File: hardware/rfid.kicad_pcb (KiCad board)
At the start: 2 copper layers, 29 parts, among them P1 CONN_01X02, P2 COMMS, U1 CR95HF, X1 27.12MHz

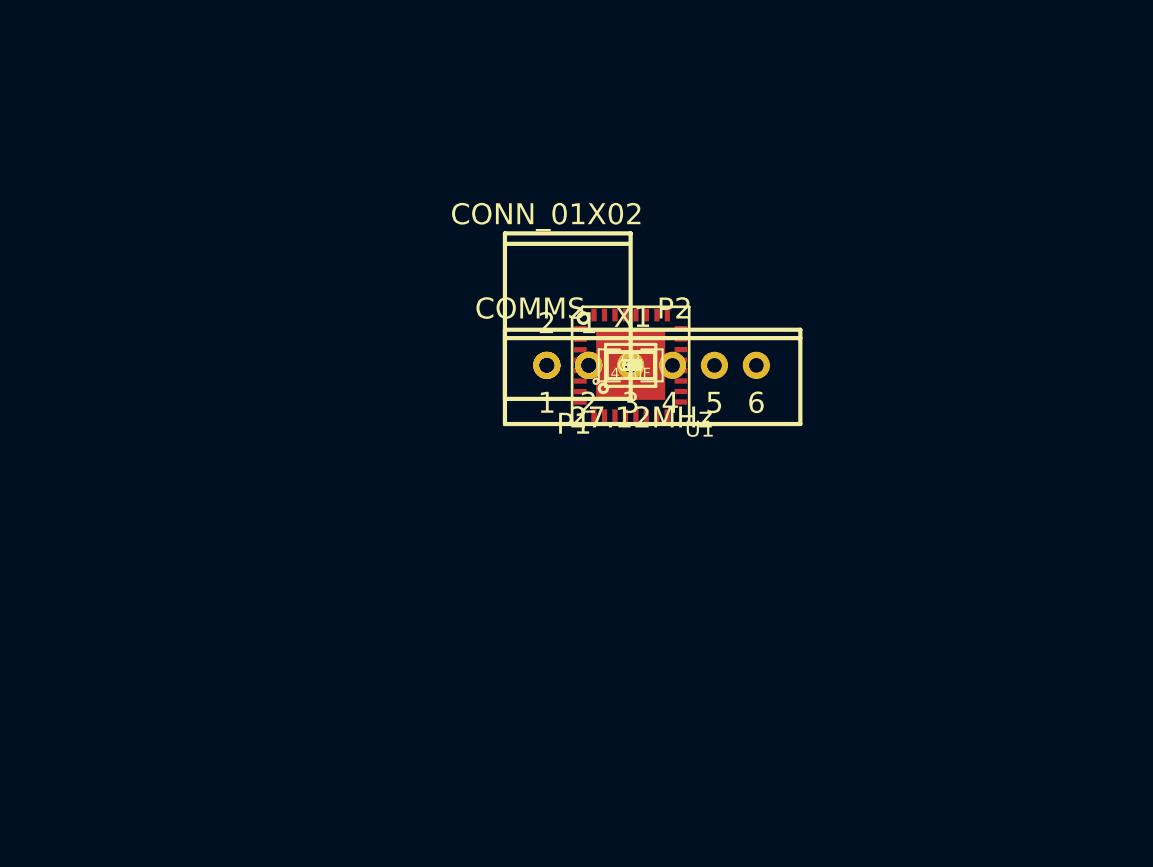
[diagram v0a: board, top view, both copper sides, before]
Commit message: Started placing components on PCB. They are just spread out currently.
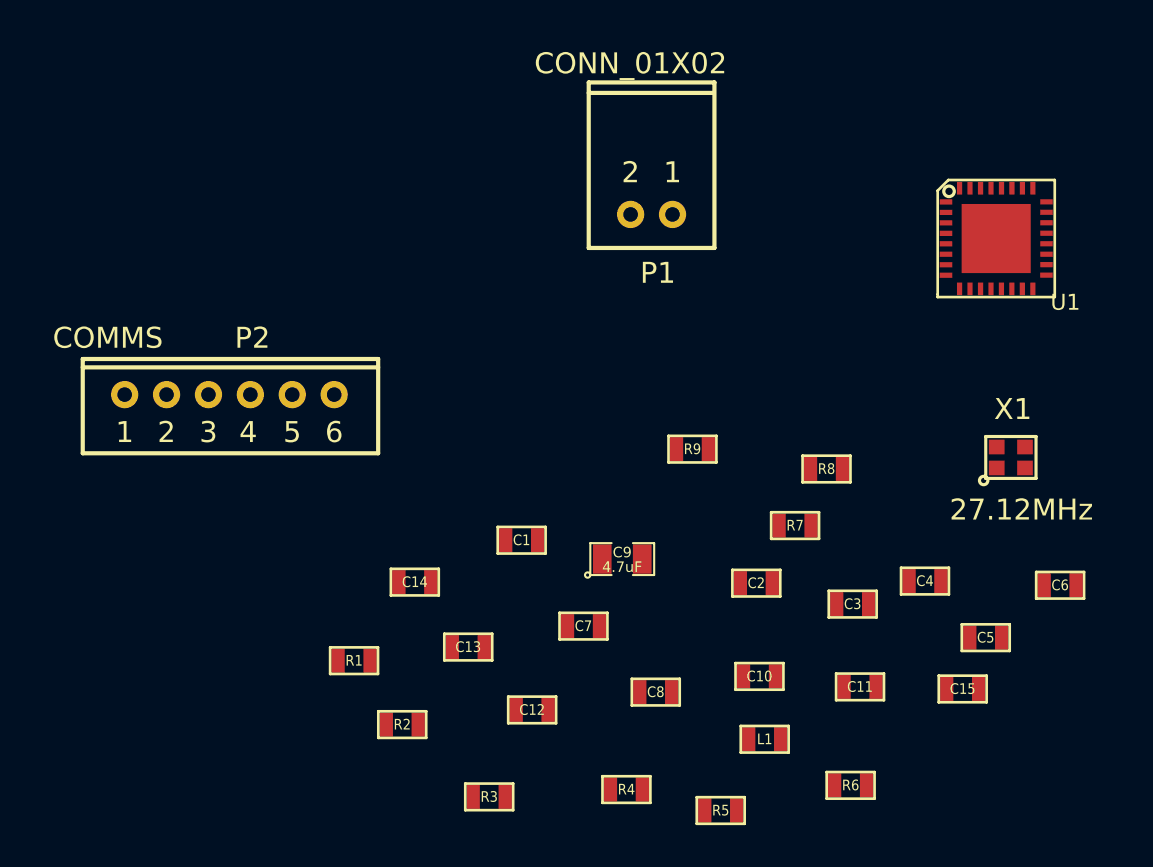
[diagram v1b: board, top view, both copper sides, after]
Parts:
- moved C6 23.0 mm to (169.0, 115.5)
- moved R6 22.6 mm to (159.0, 125.0)
- moved C15 22.1 mm to (164.3, 120.5)
- moved R5 21.7 mm to (152.8, 126.2)
- moved R3 21.7 mm to (141.8, 125.6)
- moved C5 21.4 mm to (165.4, 118.0)
- moved R2 20.3 mm to (137.6, 122.2)
- moved R4 20.2 mm to (148.3, 125.2)
- moved P2 20.2 mm to (128.3, 106.4)
- moved R1 19.3 mm to (135.3, 119.1)
- moved L1 19.0 mm to (154.9, 122.8)
- moved C11 18.9 mm to (159.4, 120.3)
- moved X1 18.7 mm to (166.7, 109.4)
- moved U1 18.5 mm to (165.9, 99.0)
- moved C4 17.4 mm to (162.6, 115.3)
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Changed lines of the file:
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@@
 (kicad_pcb (version 4) (host pcbnew "(2014-09-17 BZR 5140)-product")
   (general
-    (links 0)
-    (no_connects 0)
-    (area 0 0 0 0)
+    (links 60)
+    (no_connects 33)
+    (area 139.338767 96.6246 156.955101 108.9025)
     (thickness 1.6)
     (drawings 0)
@@
     (uvia_dia 0.508)
     (uvia_drill 0.127)
-  )
-  (module SMD_Packages:SMD-0603 (layer F.Cu)
-    (at 148.5011 105.0036)
+    (add_net 3V3)
+    (add_net 3V3_RF)
+    (add_net GND)
+    (add_net "Net-(C1-Pad1)")
+    (add_net "Net-(C10-Pad2)")
+    (add_net "Net-(C11-Pad2)")
+    (add_net "Net-(C12-Pad1)")
+    (add_net "Net-(C13-Pad1)")
+    (add_net "Net-(C2-Pad1)")
+    (add_net "Net-(C7-Pad1)")
+    (add_net "Net-(P2-Pad1)")
+    (add_net "Net-(P2-Pad2)")
+    (add_net "Net-(P2-Pad3)")
+    (add_net "Net-(P2-Pad4)")
+    (add_net "Net-(P2-Pad5)")
+    (add_net "Net-(P2-Pad6)")
+    (add_net "Net-(R2-Pad1)")
+    (add_net "Net-(R3-Pad1)")
+    (add_net "Net-(R5-Pad2)")
+    (add_net "Net-(R6-Pad2)")
+    (add_net "Net-(R7-Pad2)")
+    (add_net "Net-(R8-Pad2)")
+    (add_net "Net-(U1-Pad10)")
+    (add_net "Net-(U1-Pad11)")
+    (add_net "Net-(U1-Pad23)")
+    (add_net "Net-(U1-Pad24)")
+    (add_net "Net-(U1-Pad25)")
+    (add_net "Net-(U1-Pad26)")
+    (add_net "Net-(U1-Pad27)")
+    (add_net "Net-(U1-Pad28)")
+    (add_net "Net-(U1-Pad3)")
+    (add_net "Net-(U1-Pad4)")
+    (add_net "Net-(U1-Pad7)")
+    (add_net "Net-(X1-Pad2)")
+    (add_net "Net-(X1-Pad4)")
+  )
+  (module SMD_Packages:SMD-0603 (layer F.Cu)
+    (at 143.3 113.35)
     (attr smd)
     (fp_text reference C1 (at 0 0) (layer F.SilkS)
@@
   )
   (module SMD_Packages:SMD-0603 (layer F.Cu)
-    (at 148.5011 105.0036)
+    (at 154.5 115.4)
     (attr smd)
     (fp_text reference C2 (at 0 0) (layer F.SilkS)
@@
   )
   (module SMD_Packages:SMD-0603 (layer F.Cu)
-    (at 148.5011 105.0036)
+    (at 159.1 116.4)
     (attr smd)
     (fp_text reference C3 (at 0 0) (layer F.SilkS)
@@
   )
   (module SMD_Packages:SMD-0603 (layer F.Cu)
-    (at 148.5011 105.0036)
+    (at 162.55 115.3)
     (attr smd)
     (fp_text reference C4 (at 0 0) (layer F.SilkS)
@@
   )
   (module SMD_Packages:SMD-0603 (layer F.Cu)
-    (at 148.5011 105.0036)
+    (at 165.45 118)
     (attr smd)
     (fp_text reference C5 (at 0 0) (layer F.SilkS)
@@
   )
   (module SMD_Packages:SMD-0603 (layer F.Cu)
-    (at 148.5011 105.0036)
+    (at 169 115.5)
     (attr smd)
     (fp_text reference C6 (at 0 0) (layer F.SilkS)
@@
   )
   (module SMD_Packages:SMD-0603 (layer F.Cu)
-    (at 148.5011 105.0036)
+    (at 146.25 117.45)
     (attr smd)
     (fp_text reference C7 (at 0 0) (layer F.SilkS)
@@
   )
   (module SMD_Packages:SMD-0603 (layer F.Cu)
-    (at 148.5011 105.0036)
+    (at 149.7 120.6)
     (attr smd)
     (fp_text reference C8 (at 0 0) (layer F.SilkS)
@@
   )
   (module SMD_Packages:SMD-0805 (layer F.Cu)
-    (at 148.5011 105.0036)
+    (at 148.1 114.25)
     (attr smd)
     (fp_text reference C9 (at 0 -0.3175) (layer F.SilkS)
@@
   )
   (module SMD_Packages:SMD-0603 (layer F.Cu)
-    (at 148.5011 105.0036)
+    (at 154.65 119.85)
     (attr smd)
     (fp_text reference C10 (at 0 0) (layer F.SilkS)
@@
   )
   (module SMD_Packages:SMD-0603 (layer F.Cu)
-    (at 148.5011 105.0036)
+    (at 159.45 120.35)
     (attr smd)
     (fp_text reference C11 (at 0 0) (layer F.SilkS)
@@
   )
   (module SMD_Packages:SMD-0603 (layer F.Cu)
-    (at 148.5011 105.0036)
+    (at 143.8 121.45)
     (attr smd)
     (fp_text reference C12 (at 0 0) (layer F.SilkS)
@@
   )
   (module SMD_Packages:SMD-0603 (layer F.Cu)
-    (at 148.5011 105.0036)
+    (at 140.75 118.45)
     (attr smd)
     (fp_text reference C13 (at 0 0) (layer F.SilkS)
@@
   )
   (module SMD_Packages:SMD-0603 (layer F.Cu)
-    (at 148.5011 105.0036)
+    (at 138.2 115.35)
     (attr smd)
     (fp_text reference C14 (at 0 0) (layer F.SilkS)
@@
   )
   (module SMD_Packages:SMD-0603 (layer F.Cu)
-    (at 148.5011 105.0036)
+    (at 164.35 120.45)
     (attr smd)
     (fp_text reference C15 (at 0 0) (layer F.SilkS)
@@
   )
   (module SMD_Packages:SMD-0603 (layer F.Cu)
-    (at 148.5011 105.0036)
+    (at 154.9 122.85)
     (attr smd)
     (fp_text reference L1 (at 0 0) (layer F.SilkS)
@@
   )
   (module rfid:JST_PH_2pin_side (layer F.Cu)
-    (at 148.5011 105.0036)
+    (at 152.5 97.8)
     (fp_text reference P1 (at -2.7 2.8) (layer F.SilkS)
       (effects (font (size 1 1) (thickness 0.15)))
@@
   )
   (module rfid:JST_PH_6pin (layer F.Cu)
-    (at 148.5011 105.0036)
+    (at 128.35 106.4)
     (fp_text reference P2 (at 2.1 -2.7) (layer F.SilkS)
       (effects (font (size 1 1) (thickness 0.15)))
@@
   )
   (module SMD_Packages:SMD-0603 (layer F.Cu)
-    (at 148.5011 105.0036)
+    (at 135.3 119.1)
     (attr smd)
     (fp_text reference R1 (at 0 0) (layer F.SilkS)
@@
   )
   (module SMD_Packages:SMD-0603 (layer F.Cu)
-    (at 148.5011 105.0036)
+    (at 137.6 122.15)
     (attr smd)
     (fp_text reference R2 (at 0 0) (layer F.SilkS)
@@
   )
   (module SMD_Packages:SMD-0603 (layer F.Cu)
-    (at 148.5011 105.0036)
+    (at 141.75 125.6)
     (attr smd)
     (fp_text reference R3 (at 0 0) (layer F.SilkS)
@@
   )
   (module SMD_Packages:SMD-0603 (layer F.Cu)
-    (at 148.5011 105.0036)
+    (at 148.3 125.25)
     (attr smd)
     (fp_text reference R4 (at 0 0) (layer F.SilkS)
@@
   )
   (module SMD_Packages:SMD-0603 (layer F.Cu)
-    (at 148.5011 105.0036)
+    (at 152.8 126.25)
     (attr smd)
     (fp_text reference R5 (at 0 0) (layer F.SilkS)
@@
   )
   (module SMD_Packages:SMD-0603 (layer F.Cu)
-    (at 148.5011 105.0036)
+    (at 159 125.05)
     (attr smd)
     (fp_text reference R6 (at 0 0) (layer F.SilkS)
@@
   )
   (module SMD_Packages:SMD-0603 (layer F.Cu)
-    (at 148.5011 105.0036)
+    (at 156.35 112.65)
     (attr smd)
     (fp_text reference R7 (at 0 0) (layer F.SilkS)
@@
   )
   (module SMD_Packages:SMD-0603 (layer F.Cu)
-    (at 148.5011 105.0036)
+    (at 157.85 109.95)
     (attr smd)
     (fp_text reference R8 (at 0 0) (layer F.SilkS)
@@
   )
   (module SMD_Packages:SMD-0603 (layer F.Cu)
-    (at 148.5011 105.0036)
+    (at 151.4511 109.0036)
     (attr smd)
     (fp_text reference R9 (at 0 0) (layer F.SilkS)
@@
   )
   (module SMD_Packages:QFN-32-1EP (layer F.Cu)
-    (at 148.5011 105.0036)
+    (at 165.95 98.95)
     (descr QFN-32-1EP)
     (attr smd)
@@
   )
   (module rfid:2x1.6_crystal (layer F.Cu)
-    (at 148.5011 105.0036)
+    (at 166.65 109.4)
     (fp_text reference X1 (at 0.1 -2.3) (layer F.SilkS)
       (effects (font (size 1 1) (thickness 0.15)))

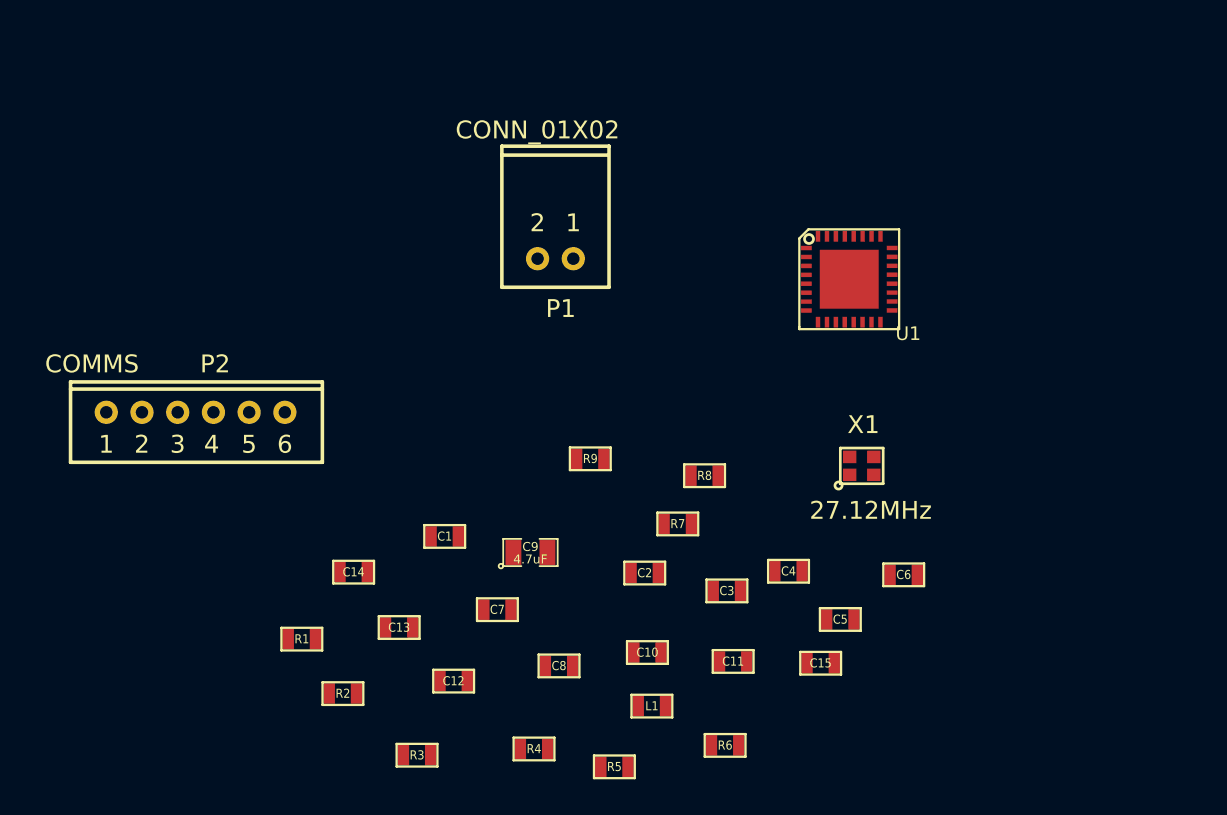
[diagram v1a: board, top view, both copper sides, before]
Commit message: Moved components around on rfid board. They are kinda where they need to go now. Need to figure out what size PCB should be before anything else.
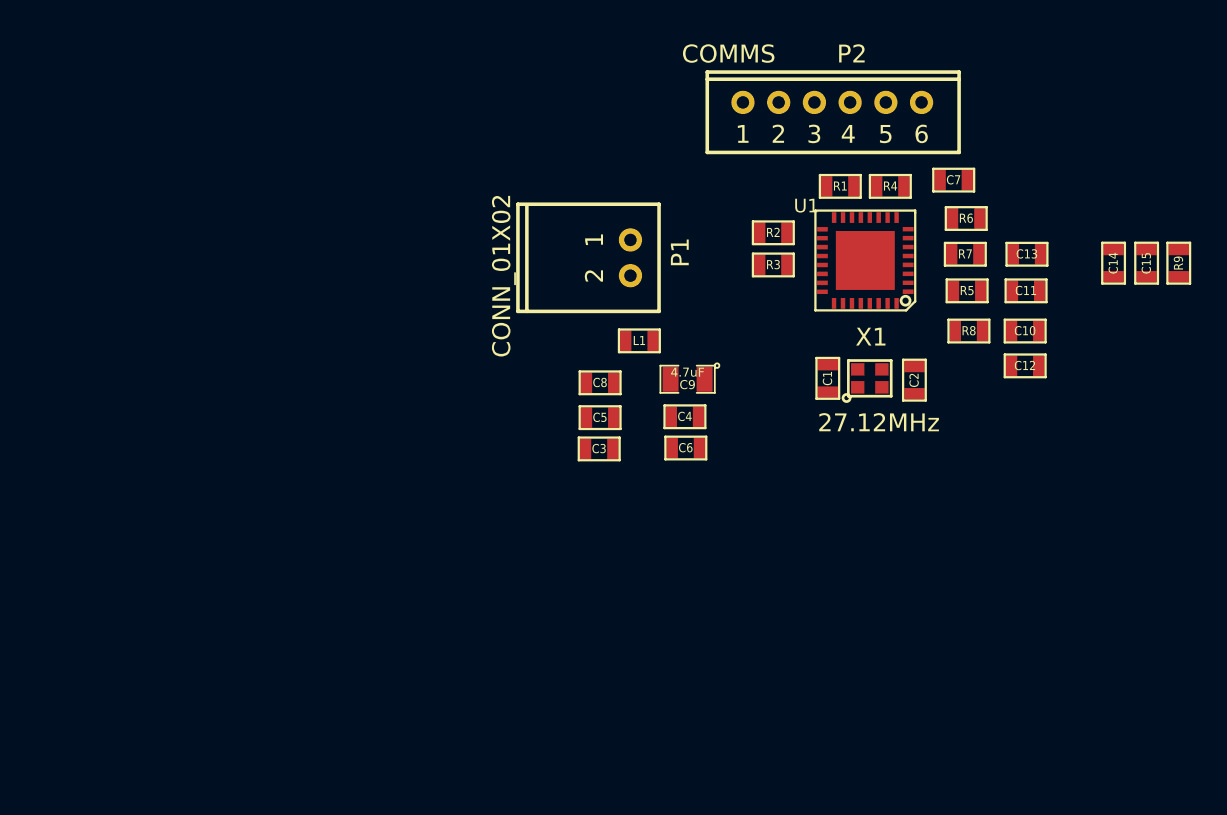
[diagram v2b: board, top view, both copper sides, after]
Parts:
- moved C14 45.9 mm to (180.8, 98.0), turned to 90 degrees
- moved C13 40.9 mm to (175.9, 97.5), turned to 180 degrees
- moved P2 39.6 mm to (164.0, 89.0)
- moved R1 39.4 mm to (165.4, 93.8), turned to 180 degrees
- moved R4 37.3 mm to (168.2, 93.8)
- moved C12 36.5 mm to (175.8, 103.8), turned to 180 degrees
- moved R2 35.3 mm to (161.7, 96.3), turned to 180 degrees
- moved C7 35.1 mm to (171.8, 93.4)
- moved R9 34.7 mm to (184.4, 98.0), turned to 90 degrees
- moved R3 33.9 mm to (161.7, 98.2), turned to 180 degrees
- moved R5 33.2 mm to (172.6, 99.6), turned to 180 degrees
- moved R6 32.4 mm to (172.5, 95.5), turned to 180 degrees
- moved C15 28.9 mm to (182.6, 98.0), turned to 90 degrees
- moved C10 27.8 mm to (175.8, 101.8), turned to 180 degrees
- moved C11 26.4 mm to (175.8, 99.6), turned to 180 degrees
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
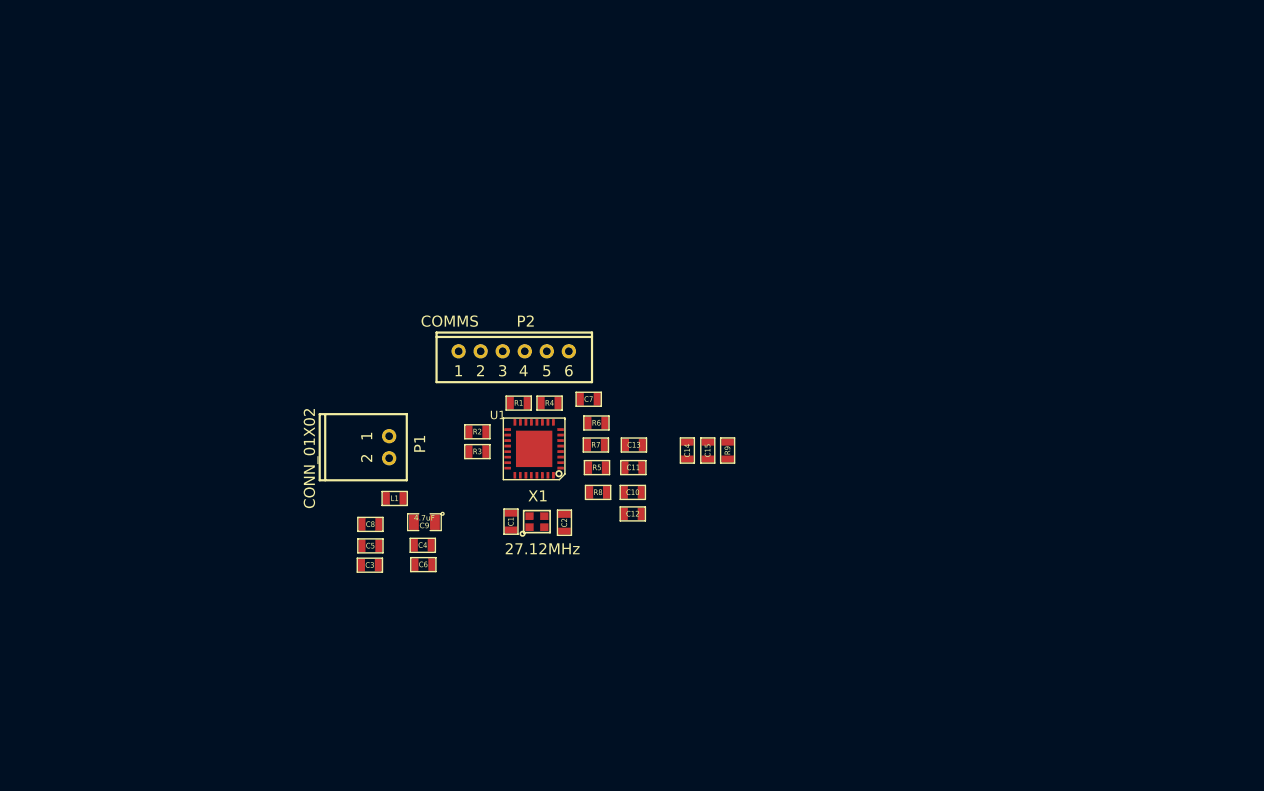
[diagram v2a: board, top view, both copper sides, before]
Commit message: Created board outline for rfid board (5cmX7.5cm). Added four 3.5mm mounting holes on a 4cmX6.5cm centers. Added ~420nH square antenna to board as well.
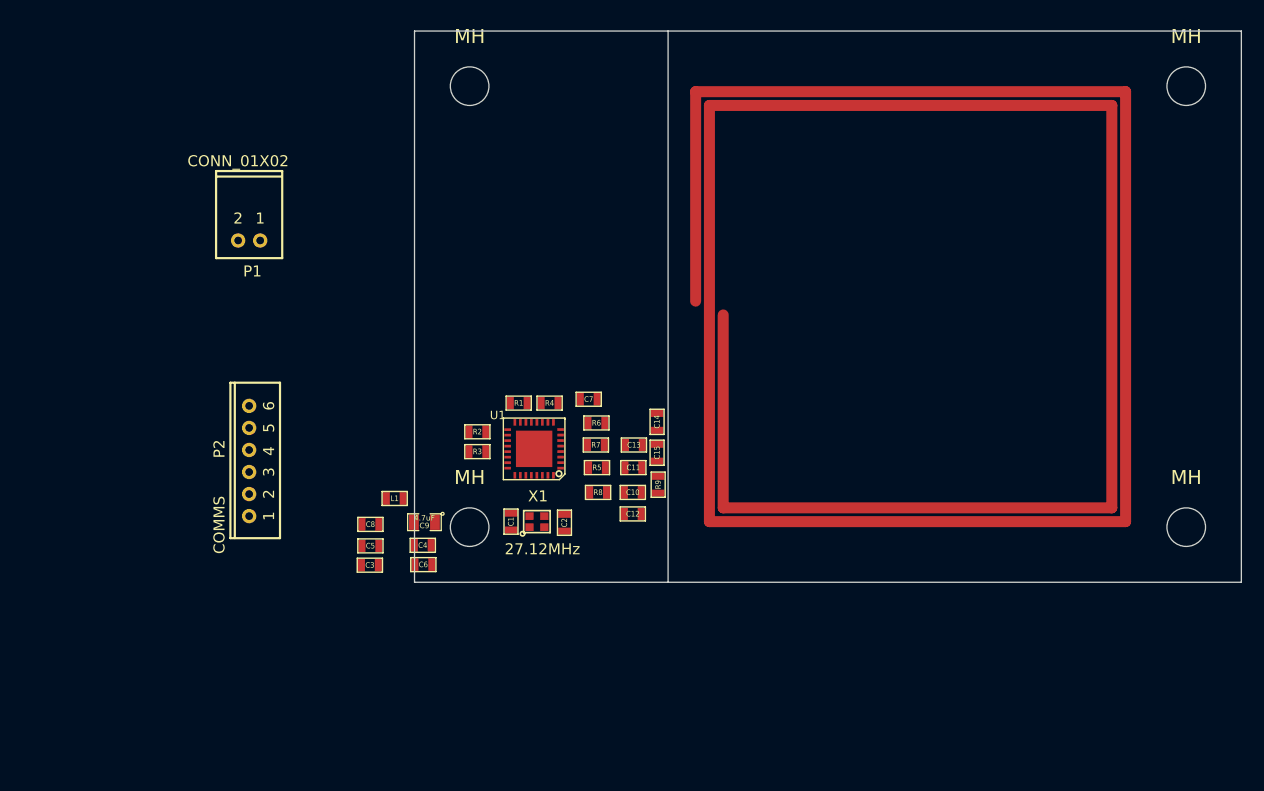
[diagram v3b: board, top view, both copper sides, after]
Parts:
- added MH: MountingHole_3-5mm_RevA_Date21Jun2010, Mounting_Holes:MountingHole_3-5mm, F.Cu at (226.0, 65.0)
- added MH: MountingHole_3-5mm_RevA_Date21Jun2010, Mounting_Holes:MountingHole_3-5mm, F.Cu at (226.0, 105.0)
- added MH: MountingHole_3-5mm_RevA_Date21Jun2010, Mounting_Holes:MountingHole_3-5mm, F.Cu at (161.0, 105.0)
- added MH: MountingHole_3-5mm_RevA_Date21Jun2010, Mounting_Holes:MountingHole_3-5mm, F.Cu at (161.0, 65.0)
- moved P2 25.5 mm to (141.0, 100.0), turned to 90 degrees
- moved P1 18.5 mm to (144.0, 79.0), turned to 0 degrees
- moved R9 7.02 mm to (178.1, 101.2)
- moved C15 4.60 mm to (178.0, 98.2)
- moved C14 3.78 mm to (178.0, 95.5)
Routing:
- net (no net): track 0.00 -> 298.2 mm
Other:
- board outline added: 75 x 50 mm
- net class Default: clearance 0.254 -> 0.15; trace_width 0.254 -> 0.25; via_dia 0.889 -> 0.6; via_drill 0.635 -> 0.3
- rule trace_clearance: 0.254 -> 0.15
- rule trace_min: 0.254 -> 0.15
- rule via_min_drill: 0.508 -> 0.3
- rule via_min_size: 0.889 -> 0.6
